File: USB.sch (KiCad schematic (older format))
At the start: 49 parts, among them J1 USB_C_Receptacle, J7 USB_MICRO_B, U1 MIMX8MM6DVTLZAA, U11 AP2411SN-7, U2 CYPD4155-96BZXI, U6 SN65DSI86ZQER, U9 NX20P3483UK

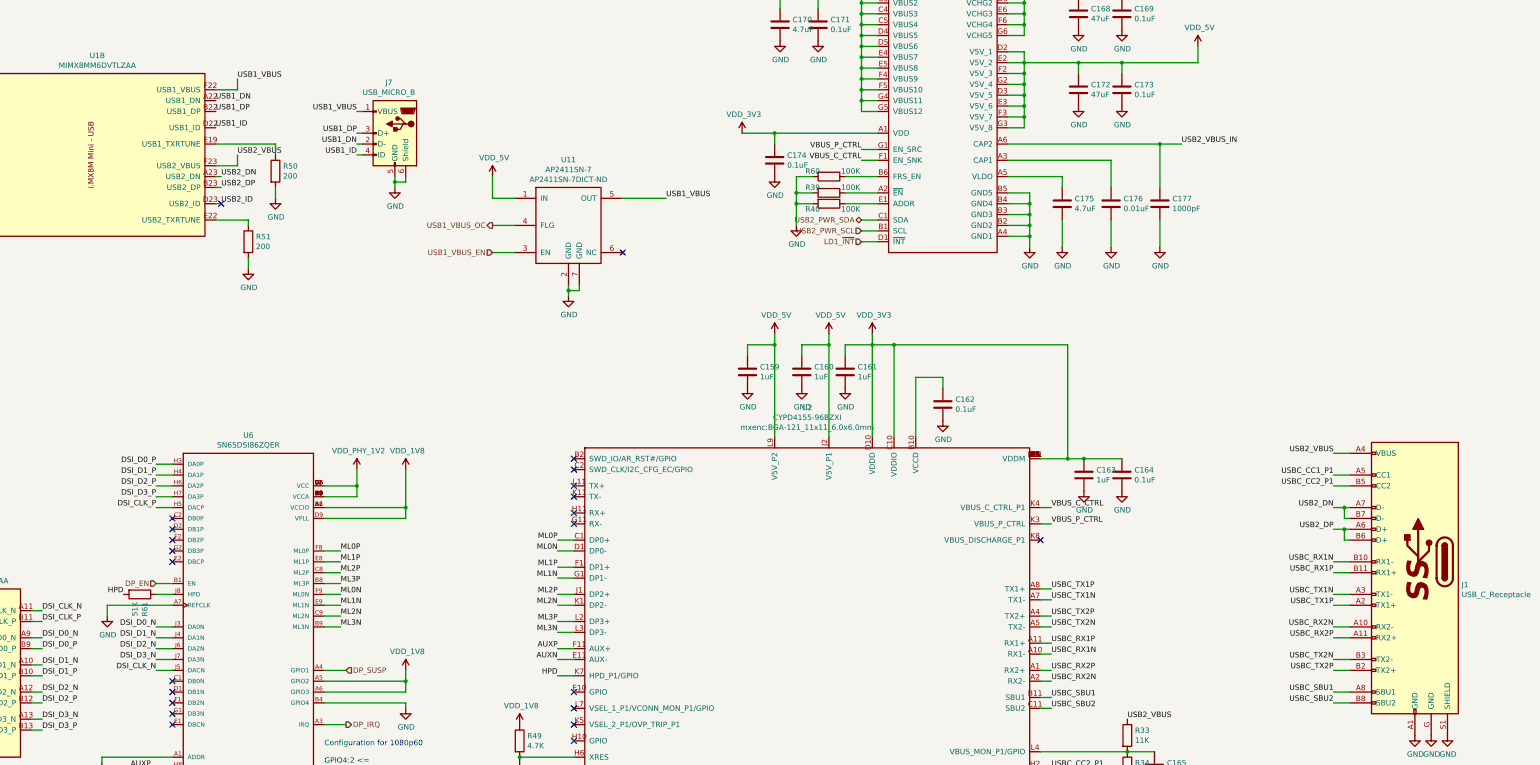
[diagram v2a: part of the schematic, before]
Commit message: Add esd protection for usb
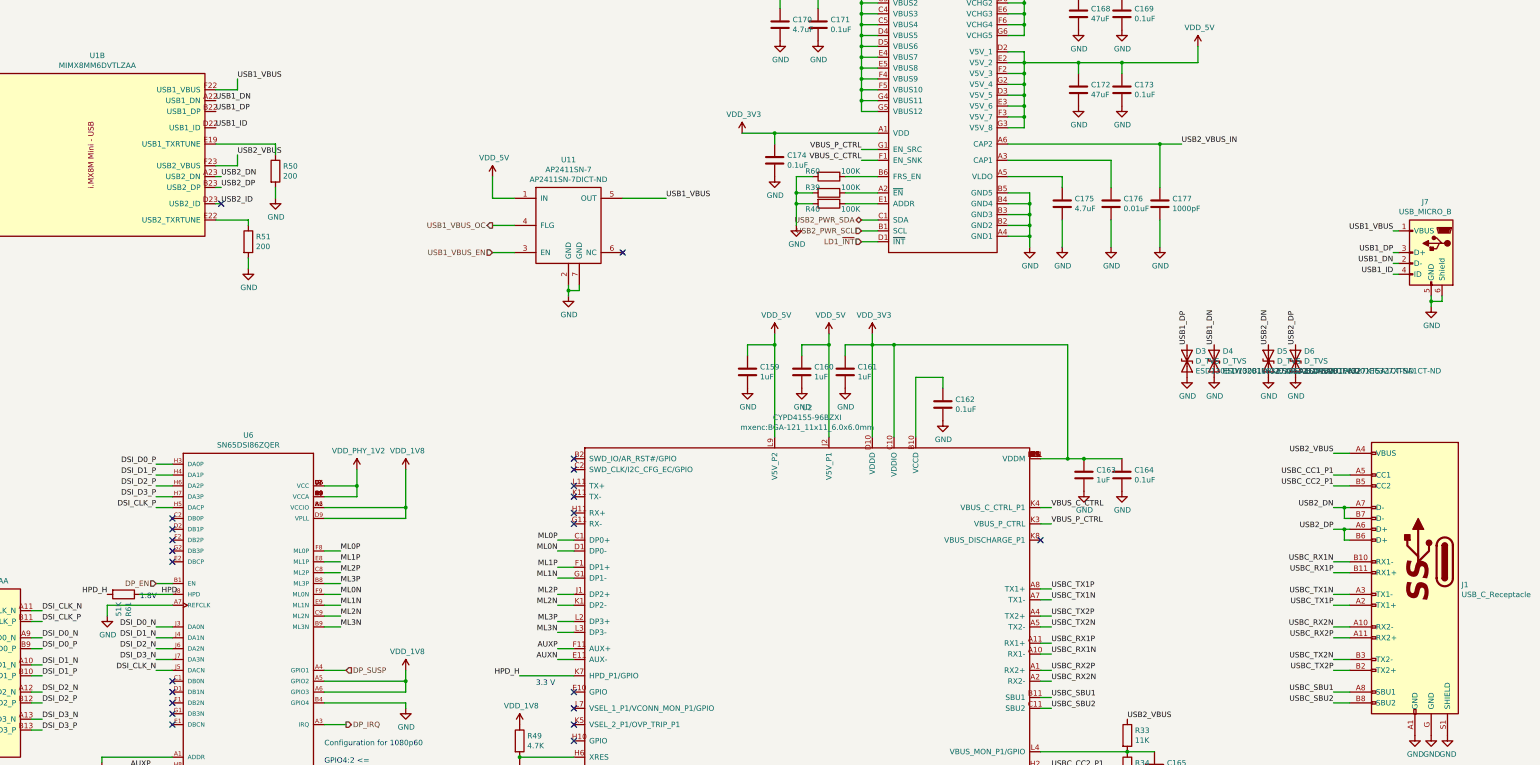
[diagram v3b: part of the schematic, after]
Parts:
- added D3, D4, D5, D6: D_TVS, Diode_SMD:D_0201_0603Metric, symbol Device:D_TVS
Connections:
- net GND: now also D3.2 (A2), D4.2 (A2), D5.2 (A2), D6.2 (A2)
- net HPD: now also R61.1, U6.J8 (HPD); no longer R61.2, U2.K7 (HPD_P1/GPIO)
- net USB1_DN: now also D4.1 (A1)
- net USB1_DP: now also D3.1 (A1)
- net USB2_DN: now also D5.1 (A1)
- net USB2_DP: now also D6.1 (A1)
- new net HPD_H: R61.2, U2.K7 (HPD_P1/GPIO)
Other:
- note added: "1.8V"
- note added: "3.3 V"
- moved on the sheet: J7, R61
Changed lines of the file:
@@
 Wire Wire Line
 	14200 5400 14350 5400
-Text Label 3050 6700 2    50   ~ 0
-HPD
-Text Label 7050 7450 2    50   ~ 0
-HPD
-Wire Wire Line
-	7050 7450 7200 7450
-Wire Wire Line
-	5200 2650 5250 2650
-Wire Wire Line
-	5250 2450 5200 2450
-Wire Wire Line
-	5200 2550 5250 2550
+Text Label 2900 6700 2    50   ~ 0
+HPD_H
+Text Label 6700 7450 2    50   ~ 0
+HPD_H
+Wire Wire Line
+	14750 3750 14800 3750
 $Comp
 L Connector:USB_B_Micro J?
 U 1 1 5D67C52A
-P 5550 2450
+P 15100 3550
 AR Path="/5D67C52A" Ref="J?"  Part="1"
 AR Path="/5D6742B7/5D67C52A" Ref="J7"  Part="1"
-F 0 "J7" H 5605 2917 50  0000 C CNN
-F 1 "USB_MICRO_B" H 5605 2826 50  0000 C CNN
-F 2 "Connector_USB:USB_Micro-B_Molex_47346-0001" H 5700 2400 50  0001 C CNN
-F 3 " ~" H 5700 2400 50  0001 C CNN
-	1    5550 2450
+F 0 "J7" H 15155 4017 50  0000 C CNN
+F 1 "USB_MICRO_B" H 15155 3926 50  0000 C CNN
+F 2 "Connector_USB:USB_Micro-B_Molex_47346-0001" H 15250 3500 50  0001 C CNN
+F 3 " ~" H 15250 3500 50  0001 C CNN
+	1    15100 3550
 	-1   0    0    -1
 $EndComp
@@
 Text Label 3950 2850 0    50   ~ 0
 USB2_DN
-Text Label 5200 2550 2    50   ~ 0
+Text Label 14750 3650 2    50   ~ 0
 USB1_DN
-Text Label 5200 2450 2    50   ~ 0
+Text Label 14750 3550 2    50   ~ 0
 USB1_DP
-Text Label 5200 2650 2    50   ~ 0
+Text Label 14750 3750 2    50   ~ 0
 USB1_ID
 Text Label 11600 6050 0    50   ~ 0
@@
 L power:GND #PWR0232
 U 1 1 5DBB4115
-P 5550 2950
-F 0 "#PWR0232" H 5550 2700 50  0001 C CNN
-F 1 "GND" H 5555 2777 50  0000 C CNN
-F 2 "" H 5550 2950 50  0001 C CNN
-F 3 "" H 5550 2950 50  0001 C CNN
-	1    5550 2950
-	1    0    0    -1
-$EndComp
-Wire Wire Line
-	5550 2950 5550 2900
-Wire Wire Line
-	5650 2850 5650 2900
-Wire Wire Line
-	5650 2900 5550 2900
-Connection ~ 5550 2900
-Wire Wire Line
-	5550 2900 5550 2850
+P 15100 4050
+F 0 "#PWR0232" H 15100 3800 50  0001 C CNN
+F 1 "GND" H 15105 3877 50  0000 C CNN
+F 2 "" H 15100 4050 50  0001 C CNN
+F 3 "" H 15100 4050 50  0001 C CNN
+	1    15100 4050
+	1    0    0    -1
+$EndComp
+Wire Wire Line
+	15100 4050 15100 4000
+Wire Wire Line
+	15200 3950 15200 4000
+Wire Wire Line
+	15200 4000 15100 4000
+Connection ~ 15100 4000
+Wire Wire Line
+	15100 4000 15100 3950
 $Comp
 L Device:R R51
@@
 	8050 3050 7650 3050
 Wire Wire Line
-	5250 2250 5200 2250
+	14800 3350 14750 3350
 Text Label 4100 1950 0    50   ~ 0
 USB1_VBUS
@@
 Wire Wire Line
 	4100 2750 3900 2750
-Text Label 5200 2250 2    50   ~ 0
+Text Label 14750 3350 2    50   ~ 0
 USB1_VBUS
 NoConn ~ 7650 3550
@@
 Text HLabel 6450 3300 0    50   Output ~ 0
 USB1_VBUS_OC
-Wire Wire Line
-	6450 3300 6650 3300
 Text HLabel 6450 3550 0    50   Input ~ 0
 USB1_VBUS_EN
@@
 	3350 6600 3500 6600
 Wire Wire Line
-	3350 6700 3500 6700
+	3200 6700 3500 6700
 $Comp
 L Device:R R61
 U 1 1 5EBEB8C9
-P 3200 6700
-F 0 "R61" H 3270 6746 50  0000 L CNN
-F 1 "51K" H 3270 6655 50  0000 L CNN
-F 2 "Resistor_SMD:R_0201_0603Metric" V 3130 6700 50  0001 C CNN
-F 3 "~" H 3200 6700 50  0001 C CNN
-	1    3200 6700
+P 3050 6700
+F 0 "R61" H 3120 6746 50  0000 L CNN
+F 1 "51K" H 3120 6655 50  0000 L CNN
+F 2 "Resistor_SMD:R_0201_0603Metric" V 2980 6700 50  0001 C CNN
+F 3 "~" H 3050 6700 50  0001 C CNN
+	1    3050 6700
 	0    1    1    0
 $EndComp
@@
 Wire Wire Line
 	12950 1650 12950 1800
+Wire Wire Line
+	6450 3300 6650 3300
+Wire Wire Line
+	7200 7450 6700 7450
+Text Notes 6850 7550 0    50   ~ 0
+3.3 V
+Text Label 3400 6700 0    50   ~ 0
+HPD
+Text Notes 3200 6750 0    50   ~ 0
+1.8V
+Wire Wire Line
+	14800 3550 14750 3550
+Wire Wire Line
+	14750 3650 14800 3650
+Text Label 13100 4400 1    50   ~ 0
+USB1_DN
+$Comp
+L Device:D_TVS D3
+U 1 1 5DDAD331
+P 12850 4550
+F 0 "D3" V 12759 4629 50  0000 L CNN
+F 1 "D_TVS" V 12850 4629 50  0000 L CNN
+F 2 "Diode_SMD:D_0201_0603Metric" H 12850 4550 50  0001 C CNN
+F 3 "~" H 12850 4550 50  0001 C CNN
+F 4 "ESD130B1W0201E6327XTSA1CT-ND" V 12941 4629 50  0000 L CNN "Vendorpart"
+	1    12850 4550
+	0    1    1    0
+$EndComp
+Text Label 12850 4400 1    50   ~ 0
+USB1_DP
+$Comp
+L power:GND #PWR0263
+U 1 1 5DE0780F
+P 13100 4700
+F 0 "#PWR0263" H 13100 4450 50  0001 C CNN
+F 1 "GND" H 13105 4527 50  0000 C CNN
+F 2 "" H 13100 4700 50  0001 C CNN
+F 3 "" H 13100 4700 50  0001 C CNN
+	1    13100 4700
+	1    0    0    -1
+$EndComp
+$Comp
+L power:GND #PWR0264
+U 1 1 5DE07D77
+P 12850 4700
+F 0 "#PWR0264" H 12850 4450 50  0001 C CNN
+F 1 "GND" H 12855 4527 50  0000 C CNN
+F 2 "" H 12850 4700 50  0001 C CNN
+F 3 "" H 12850 4700 50  0001 C CNN
+	1    12850 4700
+	1    0    0    -1
+$EndComp
+Text Label 13600 4400 1    50   ~ 0
+USB2_DN
+Text Label 13850 4400 1    50   ~ 0
+USB2_DP
+$Comp
+L power:GND #PWR0265
+U 1 1 5DE08DAB
+P 13600 4700
+F 0 "#PWR0265" H 13600 4450 50  0001 C CNN
+F 1 "GND" H 13605 4527 50  0000 C CNN
+F 2 "" H 13600 4700 50  0001 C CNN
+F 3 "" H 13600 4700 50  0001 C CNN
+	1    13600 4700
+	1    0    0    -1
+$EndComp
+$Comp
+L power:GND #PWR0266
+U 1 1 5DE092E0
+P 13850 4700
+F 0 "#PWR0266" H 13850 4450 50  0001 C CNN
+F 1 "GND" H 13855 4527 50  0000 C CNN
+F 2 "" H 13850 4700 50  0001 C CNN
+F 3 "" H 13850 4700 50  0001 C CNN
+	1    13850 4700
+	1    0    0    -1
+$EndComp
+$Comp
+L Device:D_TVS D4
+U 1 1 5DEB5268
+P 13100 4550
+F 0 "D4" V 13009 4629 50  0000 L CNN
+F 1 "D_TVS" V 13100 4629 50  0000 L CNN
+F 2 "Diode_SMD:D_0201_0603Metric" H 13100 4550 50  0001 C CNN
+F 3 "~" H 13100 4550 50  0001 C CNN
+F 4 "ESD130B1W0201E6327XTSA1CT-ND" V 13191 4629 50  0000 L CNN "Vendorpart"
+	1    13100 4550
+	0    1    1    0
+$EndComp
+$Comp
+L Device:D_TVS D5
+U 1 1 5DEB554F
+P 13600 4550
+F 0 "D5" V 13509 4629 50  0000 L CNN
+F 1 "D_TVS" V 13600 4629 50  0000 L CNN
+F 2 "Diode_SMD:D_0201_0603Metric" H 13600 4550 50  0001 C CNN
+F 3 "~" H 13600 4550 50  0001 C CNN
+F 4 "ESD130B1W0201E6327XTSA1CT-ND" V 13691 4629 50  0000 L CNN "Vendorpart"
+	1    13600 4550
+	0    1    1    0
+$EndComp
+$Comp
+L Device:D_TVS D6
+U 1 1 5DEB5B9A
+P 13850 4550
+F 0 "D6" V 13759 4629 50  0000 L CNN
+F 1 "D_TVS" V 13850 4629 50  0000 L CNN
+F 2 "Diode_SMD:D_0201_0603Metric" H 13850 4550 50  0001 C CNN
+F 3 "~" H 13850 4550 50  0001 C CNN
+F 4 "ESD130B1W0201E6327XTSA1CT-ND" V 13941 4629 50  0000 L CNN "Vendorpart"
+	1    13850 4550
+	0    1    1    0
+$EndComp
 $EndSCHEMATC

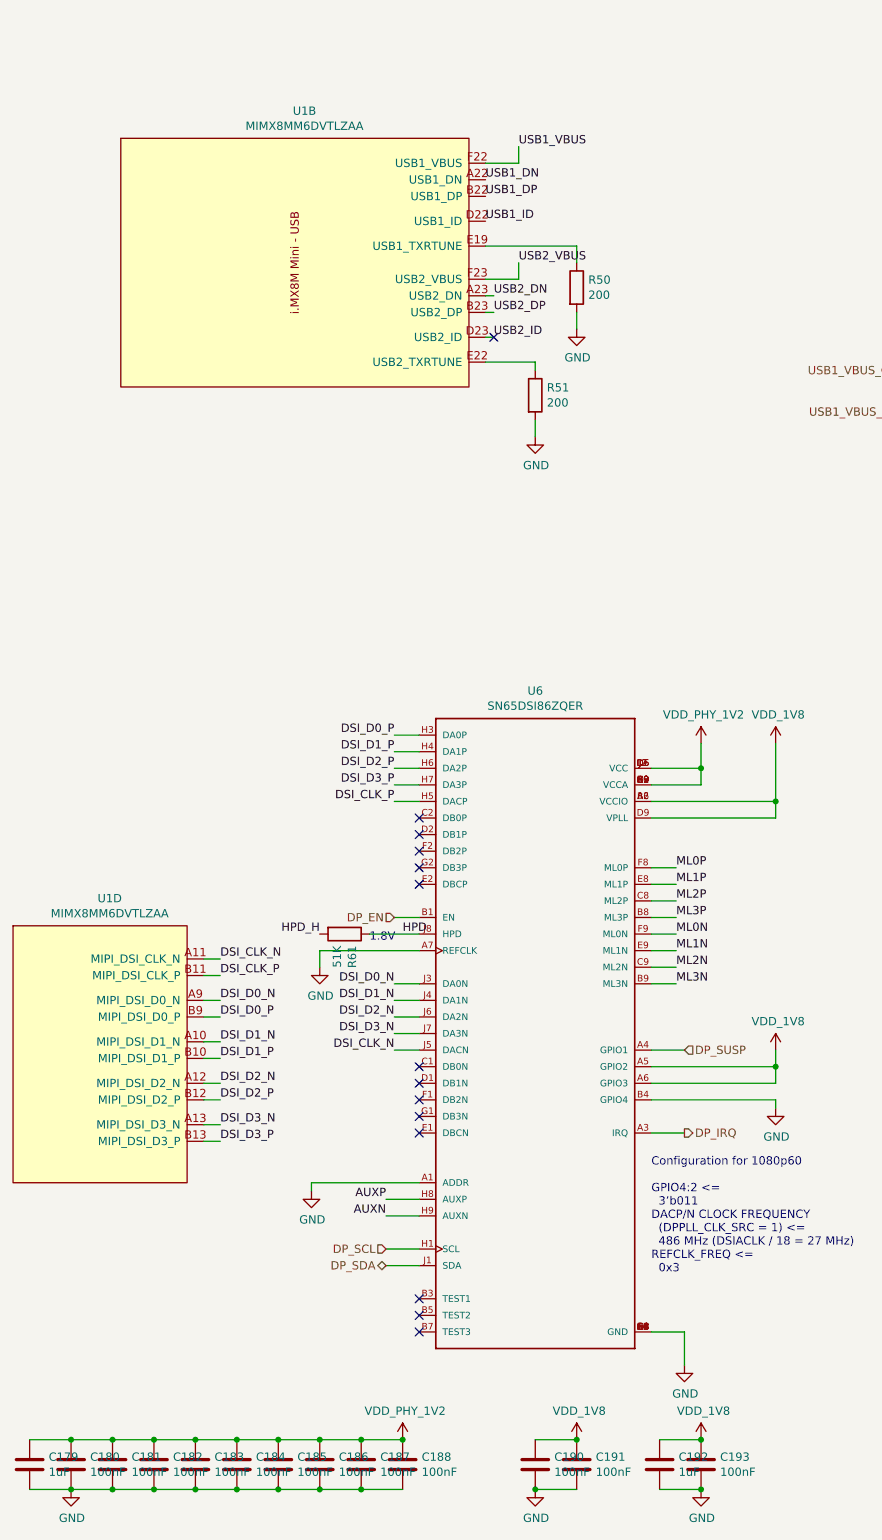
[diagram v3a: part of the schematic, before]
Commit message: Complete entry of bom
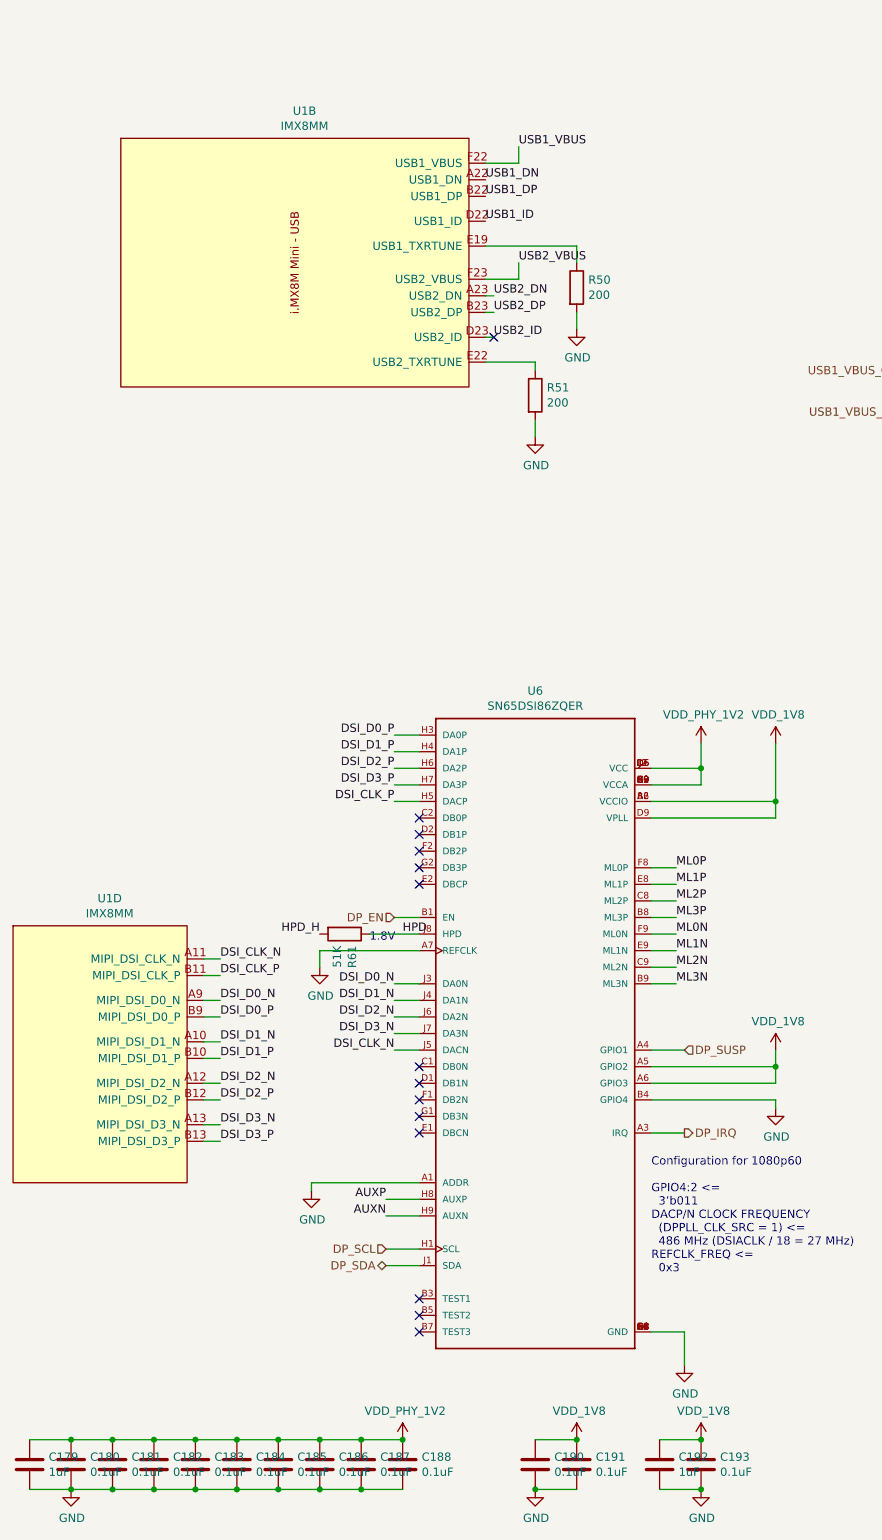
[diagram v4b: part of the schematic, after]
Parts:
- C159, C160, C161, C163, C179, C192: Mfgr (none) -> Murata; Part (none) -> GRM033C80G105ME05D; Vendorpart (none) -> 490-18622-1-ND
- C162, C164, C165, C178: Mfgr (none) -> Murata; Part (none) -> GRM033C80J104KE15D; Vendorpart (none) -> 490-10390-1-ND
- C168, C172: Mfgr (none) -> Murata; Part (none) -> GRM32EC81C476ME15L; Vendorpart (none) -> 490-9968-1-ND
- C169, C171, C173, C174: Mfgr (none) -> Murata; Part (none) -> GRM155R71E104KE14J; Vendorpart (none) -> 490-14603-1-ND
- C170: Mfgr (none) -> Yageo; Part (none) -> CC1210MKX7R6BB475; Vendorpart (none) -> 311-3539-1-ND
- C175: Mfgr (none) -> Taiyo Yuden; Part (none) -> JMK107C6475MA-T; Vendorpart (none) -> 587-4905-1-ND
- C176: Mfgr (none) -> Murata; Part (none) -> GRM033R71C103KE14D; Vendorpart (none) -> 490-14453-1-ND
- C177: Mfgr (none) -> Murata; Part (none) -> GRM033R71H102KA12J; Vendorpart (none) -> 490-14573-1-ND
- C180, C181, C182, C183, C184, C185, C186, C187, C188, C190, C191, C193: value 100nF -> 0.1uF; Mfgr (none) -> Murata; Part (none) -> GRM033C80J104KE15D; Vendorpart (none) -> 490-10390-1-ND
- D3, D4, D5, D6: Mfgr (none) -> Infineon; Part (none) -> ESD130B1W0201E6327XTSA1
- J1: Mfgr (none) -> JAE; Part (none) -> DX07S024JJ2R1300; Vendorpart (none) -> 670-2794-1-ND
- J7: Mfgr (none) -> Molex; Part (none) -> 0473460001; Vendorpart (none) -> WM17141CT-ND
- R33: Mfgr (none) -> Panasonic; Part (none) -> ERJ-1GNF1102C; Vendorpart (none) -> P122675CT-ND
- R34: Mfgr (none) -> Panasonic; Part (none) -> ERJ-1GNF1001C; Vendorpart (none) -> P122413CT-ND
- R39, R40, R60: Mfgr (none) -> Yageo; Part (none) -> RC0201JR-07100KL; Vendorpart (none) -> 311-100KNCT-ND
- R49: Mfgr (none) -> Yageo; Part (none) -> RC0201JR-074K7L; Vendorpart (none) -> 311-4.7KNCT-ND
- R50, R51: Mfgr (none) -> Yageo; Part (none) -> RC0201FR-07200RL; Vendorpart (none) -> YAG2495CT-ND
- R61: Mfgr (none) -> Panasonic; Part (none) -> ERJ-1GNF5102C; Vendorpart (none) -> P123052CT-ND
- U1: value MIMX8MM6DVTLZAA -> IMX8MM; Mfgr (none) -> NXP; Part (none) -> MIMX8MM6CVTKZAA; Vendorpart (none) -> 568-15276-ND
- U11: Mfgr (none) -> Diodes; Part (none) -> AP2411SN-7
- U2: Mfgr (none) -> Cypress; Part (none) -> CYPD4155-96BZXI; Vendor (none) -> Mouser; Vendorpart (none) -> 727-CYPD4155-96BZXI
- U6: Field4 Dual-Channel MIPI® DSI to Embedded DisplayPort™ _eDP _ Brid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 -> (none); Field5 BGA-64 Texas Instruments -> (none); Field6 None -> (none); Field7 SN65DSI86ZQER -> (none); Field8 Unavailable -> (none); Mfgr (none) -> TI; Part (none) -> SN65DSI86ZQER; Vendorpart (none) -> 296-40498-1-ND
- U9: Mfgr (none) -> NXP; Part (none) -> NX20P3483UK; Vendorpart (none) -> 568-15322-1-ND
